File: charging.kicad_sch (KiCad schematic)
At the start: 14 parts, among them J5 JST to Battery, U2 BQ24075RGT

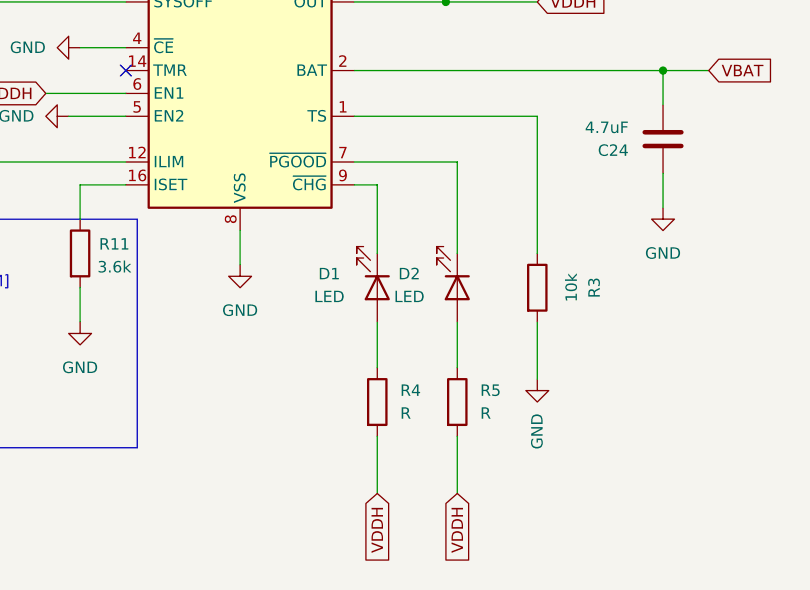
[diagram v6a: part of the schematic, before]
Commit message: Added PCB Test Layout
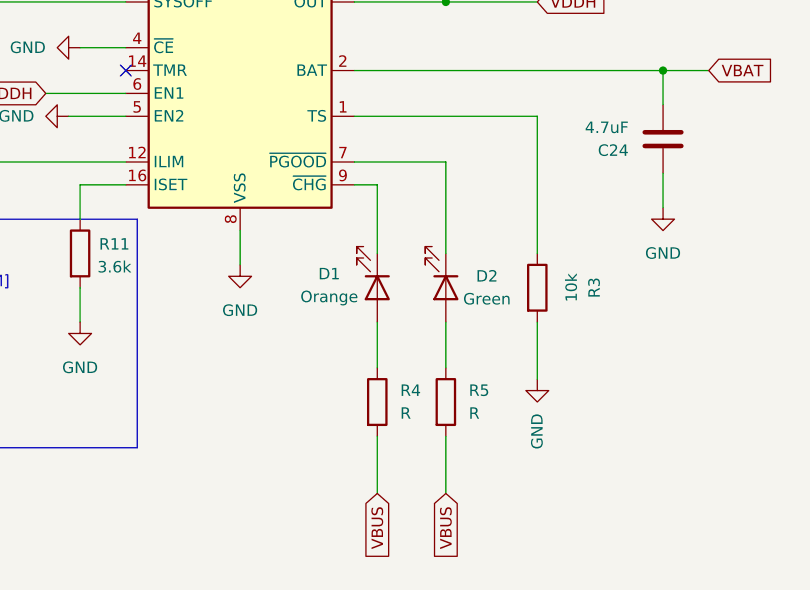
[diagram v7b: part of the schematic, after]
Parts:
- D1: value LED -> Orange; footprint (none) -> LED_SMD:LED_0805_2012Metric
- D2: value LED -> Green; footprint (none) -> LED_SMD:LED_0805_2012Metric
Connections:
- net VBUS: now also R4.2, R5.2
- net VDDH: no longer R4.2, R5.2
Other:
- moved on the sheet: D2, R5
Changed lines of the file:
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@@
-	(wire
-		(pts
-			(xy 166.37 125.73) (xy 166.37 132.08)
-		)
-		(stroke
-			(width 0)
-			(type default)
-		)
-	)
 	(wire
 		(pts
@@
 	(wire
 		(pts
+			(xy 154.94 95.25) (xy 165.1 95.25)
+		)
+		(stroke
+			(width 0)
+			(type default)
+		)
+	)
+	(wire
+		(pts
 			(xy 175.26 113.03) (xy 175.26 119.38)
 		)
@@
 	(wire
 		(pts
+			(xy 165.1 125.73) (xy 165.1 132.08)
+		)
+		(stroke
+			(width 0)
+			(type default)
+		)
+	)
+	(wire
+		(pts
 			(xy 127 60.96) (xy 130.81 60.96)
 		)
@@
 	(wire
 		(pts
-			(xy 166.37 113.03) (xy 166.37 118.11)
-		)
-		(stroke
-			(width 0)
-			(type default)
-		)
-	)
-	(wire
-		(pts
 			(xy 154.94 97.79) (xy 157.48 97.79)
 		)
@@
 	(wire
 		(pts
-			(xy 154.94 95.25) (xy 166.37 95.25)
+			(xy 165.1 95.25) (xy 165.1 105.41)
 		)
 		(stroke
@@
 	(wire
 		(pts
-			(xy 166.37 95.25) (xy 166.37 105.41)
-		)
-		(stroke
-			(width 0)
-			(type default)
-		)
-	)
-	(wire
-		(pts
 			(xy 138.43 60.96) (xy 142.24 60.96)
+		)
+		(stroke
+			(width 0)
+			(type default)
+		)
+	)
+	(wire
+		(pts
+			(xy 165.1 113.03) (xy 165.1 118.11)
 		)
 		(stroke
@@
 		)
 	)
-	(global_label "VDDH"
+	(global_label "SYSOFF_SWITCH"
 		(shape input)
-		(at 157.48 132.08 270)
+		(at 102.87 77.47 180)
 		(fields_autoplaced yes)
 		(effects
@@
 		)
 		(property "Intersheetrefs" "${INTERSHEET_REFS}"
-			(at 157.48 140.0243 90)
+			(at 85.0681 77.47 0)
 			(effects
 				(font
@@
 		)
 	)
-	(global_label "VDDH"
+	(global_label "VBAT"
 		(shape input)
-		(at 166.37 132.08 270)
+		(at 218.44 49.53 180)
 		(fields_autoplaced yes)
 		(effects
@@
 		)
 		(property "Intersheetrefs" "${INTERSHEET_REFS}"
-			(at 166.37 140.0243 90)
+			(at 211.04 49.53 0)
 			(effects
 				(font
@@
 		)
 	)
-	(global_label "SYSOFF_SWITCH"
+	(global_label "VBUS"
 		(shape input)
-		(at 102.87 77.47 180)
+		(at 157.48 132.08 270)
 		(fields_autoplaced yes)
 		(effects
@@
 		)
 		(property "Intersheetrefs" "${INTERSHEET_REFS}"
-			(at 85.0681 77.47 0)
+			(at 157.48 139.9638 90)
 			(effects
 				(font
@@
 		)
 	)
-	(global_label "VBAT"
+	(global_label "VDDH"
 		(shape input)
-		(at 218.44 49.53 180)
+		(at 175.26 77.47 0)
 		(fields_autoplaced yes)
 		(effects
@@
 				(size 1.27 1.27)
 			)
-			(justify right)
+			(justify left)
 		)
 		(property "Intersheetrefs" "${INTERSHEET_REFS}"
-			(at 211.04 49.53 0)
-			(effects
-				(font
-					(size 1.27 1.27)
-				)
-				(justify right)
-				(hide yes)
-			)
-		)
-	)
-	(global_label "VDDH"
+			(at 183.2043 77.47 0)
+			(effects
+				(font
+					(size 1.27 1.27)
+				)
+				(justify left)
+				(hide yes)
+			)
+		)
+	)
+	(global_label "VBAT"
 		(shape input)
-		(at 175.26 77.47 0)
+		(at 194.31 85.09 0)
 		(fields_autoplaced yes)
 		(effects
@@
 		)
 		(property "Intersheetrefs" "${INTERSHEET_REFS}"
-			(at 183.2043 77.47 0)
+			(at 201.71 85.09 0)
 			(effects
 				(font
@@
 		)
 	)
-	(global_label "VBAT"
+	(global_label "VBUS"
 		(shape input)
-		(at 194.31 85.09 0)
+		(at 142.24 58.42 90)
 		(fields_autoplaced yes)
 		(effects
@@
 		)
 		(property "Intersheetrefs" "${INTERSHEET_REFS}"
-			(at 201.71 85.09 0)
+			(at 142.24 50.5362 90)
 			(effects
 				(font
@@
 	(global_label "VBUS"
 		(shape input)
-		(at 142.24 58.42 90)
+		(at 165.1 132.08 270)
 		(fields_autoplaced yes)
 		(effects
@@
 				(size 1.27 1.27)
 			)
-			(justify left)
+			(justify right)
 		)
 		(property "Intersheetrefs" "${INTERSHEET_REFS}"
-			(at 142.24 50.5362 90)
-			(effects
-				(font
-					(size 1.27 1.27)
-				)
-				(justify left)
+			(at 165.1 139.9638 90)
+			(effects
+				(font
+					(size 1.27 1.27)
+				)
+				(justify right)
 				(hide yes)
 			)
@@
 			)
 		)
-		(property "Value" "LED"
+		(property "Value" "Orange"
 			(at 152.146 110.236 90)
 			(effects
@@
 			)
 		)
-		(property "Footprint" ""
+		(property "Footprint" "LED_SMD:LED_0805_2012Metric"
 			(at 157.48 109.22 0)
 			(effects
@@
 	(symbol
 		(lib_id "Device:LED")
-		(at 166.37 109.22 270)
+		(at 165.1 109.22 270)
 		(unit 1)
 		(exclude_from_sim no)
@@
 		(dnp no)
 		(property "Reference" "D2"
-			(at 161.036 107.696 90)
-			(effects
-				(font
-					(size 1.27 1.27)
-				)
-			)
-		)
-		(property "Value" "LED"
-			(at 161.036 110.236 90)
-			(effects
-				(font
-					(size 1.27 1.27)
-				)
-			)
-		)
-		(property "Footprint" ""
-			(at 166.37 109.22 0)
+			(at 169.672 107.95 90)
+			(effects
+				(font
+					(size 1.27 1.27)
+				)
+			)
+		)
+		(property "Value" "Green"
+			(at 169.672 110.49 90)
+			(effects
+				(font
+					(size 1.27 1.27)
+				)
+			)
+		)
+		(property "Footprint" "LED_SMD:LED_0805_2012Metric"
+			(at 165.1 109.22 0)
 			(effects
 				(font
@@
 		)
 		(property "Datasheet" "~"
-			(at 166.37 109.22 0)
+			(at 165.1 109.22 0)
 			(effects
 				(font
@@
 		)
 		(property "Description" "Light emitting diode"
-			(at 166.37 109.22 0)
+			(at 165.1 109.22 0)
 			(effects
 				(font
@@
 		)
 		(property "Sim.Pins" "1=K 2=A"
-			(at 166.37 109.22 0)
+			(at 165.1 109.22 0)
 			(effects
 				(font
@@
 	(symbol
 		(lib_id "Device:R")
-		(at 166.37 121.92 0)
+		(at 165.1 121.92 0)
 		(unit 1)
 		(exclude_from_sim no)
@@
 		(fields_autoplaced yes)
 		(property "Reference" "R5"
-			(at 168.91 120.6499 0)
+			(at 167.64 120.6499 0)
 			(effects
 				(font
@@
 		)
 		(property "Value" "R"
-			(at 168.91 123.1899 0)
+			(at 167.64 123.1899 0)
 			(effects
 				(font
@@
 		)
 		(property "Footprint" "Resistor_SMD:R_0603_1608Metric"
-			(at 164.592 121.92 90)
+			(at 163.322 121.92 90)
 			(effects
 				(font
@@
 		)
 		(property "Datasheet" "~"
-			(at 166.37 121.92 0)
+			(at 165.1 121.92 0)
 			(effects
 				(font
@@
 		)
 		(property "Description" "Resistor"
-			(at 166.37 121.92 0)
+			(at 165.1 121.92 0)
 			(effects
 				(font
@@
 		)
 		(instances
-			(project ""
+			(project "Slim Keyboard"
 				(path "/5d65a0d4-45a3-4af0-996a-c0381d04499a/f42a8a8a-4a34-440a-8e58-9c442fe0d23e/8d78fcfc-e335-4768-b7c7-c99d7af02414"
 					(reference "R5")

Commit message: Added actual JST connector
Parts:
- J5: value JST to Battery -> S2B-PH-SM4-TB; footprint Connector_JST:JST_PH_S2B-PH-K_1x02_P2.00mm_Horizontal -> S2B-PH-SM4-TB:JST_S2B-PH-SM4-TB; symbol Connector:Conn_01x02_Socket -> S2B-PH-SM4-TB:S2B-PH-SM4-TB; Check_prices (none) -> https://www.snapeda.com/parts/S2B-PH-SM4-TB/JST/view-part/?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; Description_1 (none) -> Connector Header Surface Mount, Right Angle 2 position 0.07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; DigiKey_Part_Number (none) -> 455-S2B-PH-SM4-TBCT-ND; MANUFACTURER (none) -> JST; MF (none) -> JST Sales; MP (none) -> S2B-PH-SM4-TB; Package (none) -> None; SnapEDA_Link (none) -> https://www.snapeda.com/parts/S2B-PH-SM4-TB/JST/view-part/?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
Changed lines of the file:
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@@
 	)
 	(symbol
-		(lib_id "Connector:Conn_01x02_Socket")
-		(at 228.6 46.99 0)
+		(lib_id "S2B-PH-SM4-TB:S2B-PH-SM4-TB")
+		(at 228.6 48.26 0)
 		(unit 1)
 		(exclude_from_sim no)
@@
 		(fields_autoplaced yes)
 		(property "Reference" "J5"
-			(at 229.87 46.9899 0)
+			(at 234.95 46.9899 0)
 			(effects
 				(font
@@
 			)
 		)
-		(property "Value" "JST to Battery"
-			(at 229.87 49.5299 0)
+		(property "Value" "S2B-PH-SM4-TB"
+			(at 234.95 49.5299 0)
 			(effects
 				(font
@@
 			)
 		)
-		(property "Footprint" "Connector_JST:JST_PH_S2B-PH-K_1x02_P2.00mm_Horizontal"
-			(at 228.6 46.99 0)
+		(property "Footprint" "S2B-PH-SM4-TB:JST_S2B-PH-SM4-TB"
+			(at 228.6 48.26 0)
 			(effects
 				(font
 					(size 1.27 1.27)
 				)
+				(justify bottom)
 				(hide yes)
 			)
 		)
-		(property "Datasheet" "~"
-			(at 228.6 46.99 0)
+		(property "Datasheet" "https://www.jst-mfg.com/product/pdf/eng/ePH.pdf"
+			(at 228.6 48.26 0)
 			(effects
 				(font
@@
 		)
 		(property "Description" "Generic connector, single row, 01x02, script generated"
-			(at 228.6 46.99 0)
+			(at 228.6 48.26 0)
 			(effects
 				(font
@@
 				(hide yes)
 			)
+		)
+		(property "DigiKey_Part_Number" "455-S2B-PH-SM4-TBCT-ND"
+			(at 228.6 48.26 0)
+			(effects
+				(font
+					(size 1.27 1.27)
+				)
+				(justify bottom)
+				(hide yes)
+			)
+		)
+		(property "SnapEDA_Link" "https://www.snapeda.com/parts/S2B-PH-SM4-TB/JST/view-part/?ref=snap"
+			(at 228.6 48.26 0)
+			(effects
+				(font
+					(size 1.27 1.27)
+				)
+				(justify bottom)
+				(hide yes)
+			)
+		)
+		(property "Description_1" "Connector Header Surface Mount, Right Angle 2 position 0.079 (2.00mm)"
+			(at 228.6 48.26 0)
+			(effects
+				(font
+					(size 1.27 1.27)
+				)
+				(justify bottom)
+				(hide yes)
+			)
+		)
+		(property "Package" "None"
+			(at 228.6 48.26 0)
+			(effects
+				(font
+					(size 1.27 1.27)
+				)
+				(justify bottom)
+				(hide yes)
+			)
+		)
+		(property "Check_prices" "https://www.snapeda.com/parts/S2B-PH-SM4-TB/JST/view-part/?ref=eda"
+			(at 228.6 48.26 0)
+			(effects
+				(font
+					(size 1.27 1.27)
+				)
+				(justify bottom)
+				(hide yes)
+			)
+		)
+		(property "MF" "JST Sales"
+			(at 228.6 48.26 0)
+			(effects
+				(font
+					(size 1.27 1.27)
+				)
+				(justify bottom)
+				(hide yes)
+			)
+		)
+		(property "MP" "S2B-PH-SM4-TB"
+			(at 228.6 48.26 0)
+			(effects
+				(font
+					(size 1.27 1.27)
+				)
+				(justify bottom)
+				(hide yes)
+			)
+		)
+		(property "MANUFACTURER" "JST"
+			(at 228.6 48.26 0)
+			(effects
+				(font
+					(size 1.27 1.27)
+				)
+				(justify bottom)
+				(hide yes)
+			)
